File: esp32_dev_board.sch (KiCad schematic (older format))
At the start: 0 parts

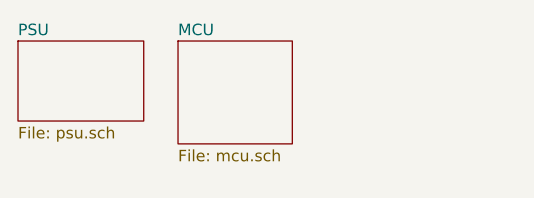
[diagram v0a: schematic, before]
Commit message: Separate MCU I/O sections in their own sheet.
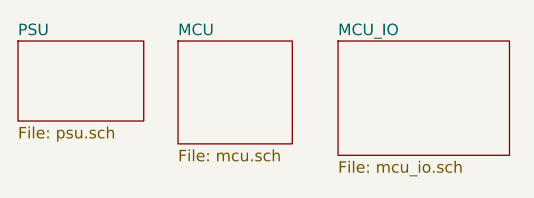
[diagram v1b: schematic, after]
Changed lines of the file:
@@
 $Descr A4 11693 8268
 encoding utf-8
-Sheet 1 3
+Sheet 1 4
 Title ""
 Date ""
@@
 F1 "mcu.sch" 50
 $EndSheet
+$Sheet
+S 2350 1200 750  500
+U 606CDE66
+F0 "MCU_IO" 50
+F1 "mcu_io.sch" 50
+$EndSheet
 $EndSCHEMATC
